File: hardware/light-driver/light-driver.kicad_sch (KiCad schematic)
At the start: 50 parts, among them J1 LED-strip0, J2 Power/CAN, J3 LED-strip1, J4 Power/CAN, J5 SWD, J6 Conn_01x08_Pin, J7 ARGB, J8 Conn_01x04_Pin, U1 TC1185-xCT, U2 TPP361061-T6TR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

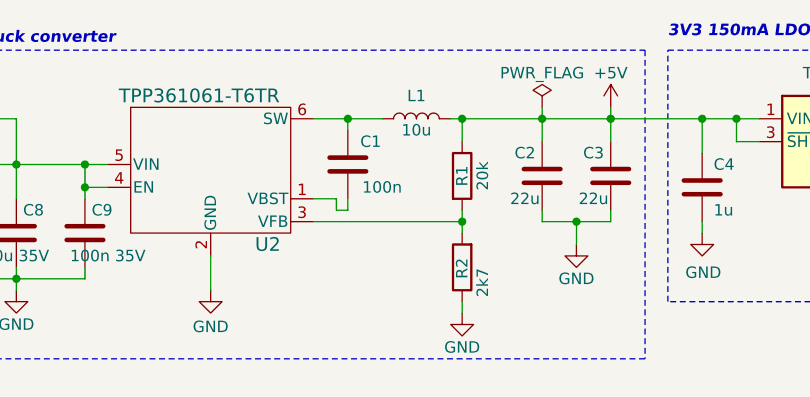
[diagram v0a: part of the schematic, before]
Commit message: Update footprints to given in inventory
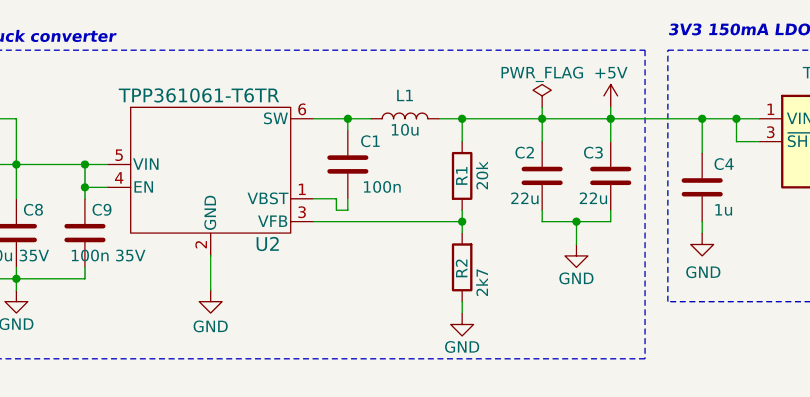
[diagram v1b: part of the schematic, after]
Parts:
- C11, C13, C2, C3, C4, C6: footprint Capacitor_SMD:C_0603_1608Metric_Pad1.08x0.95mm_HandSolder -> Capacitor_SMD:C_0805_2012Metric_Pad1.18x1.45mm_HandSolder
- L1: footprint Inductor_SMD:L_1008_2520Metric_Pad1.43x2.20mm_HandSolder -> Inductor_SMD:L_1210_3225Metric_Pad1.42x2.65mm_HandSolder
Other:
- moved on the sheet: L1
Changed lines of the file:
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@@
 	(wire
 		(pts
-			(xy 105.41 24.13) (xy 109.22 24.13)
+			(xy 105.41 24.13) (xy 107.95 24.13)
 		)
 		(stroke
@@
 	(wire
 		(pts
-			(xy 116.84 24.13) (xy 118.11 24.13)
+			(xy 115.57 24.13) (xy 118.11 24.13)
 		)
 		(stroke
@@
 			)
 		)
-		(property "Footprint" "Capacitor_SMD:C_0603_1608Metric_Pad1.08x0.95mm_HandSolder"
+		(property "Footprint" "Capacitor_SMD:C_0805_2012Metric_Pad1.18x1.45mm_HandSolder"
 			(at 208.5848 140.97 0)
 			(effects
@@
 			)
 		)
-		(property "Footprint" "Capacitor_SMD:C_0603_1608Metric_Pad1.08x0.95mm_HandSolder"
+		(property "Footprint" "Capacitor_SMD:C_0805_2012Metric_Pad1.18x1.45mm_HandSolder"
 			(at 133.6548 26.67 0)
 			(effects
@@
 			)
 		)
-		(property "Footprint" "Capacitor_SMD:C_0603_1608Metric_Pad1.08x0.95mm_HandSolder"
+		(property "Footprint" "Capacitor_SMD:C_0805_2012Metric_Pad1.18x1.45mm_HandSolder"
 			(at 188.9252 148.59 0)
 			(effects
@@
 	(symbol
 		(lib_id "Device:L")
-		(at 113.03 24.13 90)
+		(at 111.76 24.13 90)
 		(unit 1)
 		(exclude_from_sim no)
@@
 		(dnp no)
 		(property "Reference" "L1"
-			(at 113.03 21.59 90)
+			(at 111.76 21.59 90)
 			(effects
 				(font
@@
 		)
 		(property "Value" "10u"
-			(at 113.03 25.4 90)
+			(at 111.76 25.4 90)
 			(effects
 				(font
@@
 			)
 		)
-		(property "Footprint" "Inductor_SMD:L_1008_2520Metric_Pad1.43x2.20mm_HandSolder"
-			(at 113.03 24.13 0)
+		(property "Footprint" "Inductor_SMD:L_1210_3225Metric_Pad1.42x2.65mm_HandSolder"
+			(at 111.76 24.13 0)
 			(effects
 				(font
@@
 		)
 		(property "Datasheet" "~"
-			(at 113.03 24.13 0)
+			(at 111.76 24.13 0)
 			(effects
 				(font
@@
 		)
 		(property "Description" "Inductor"
-			(at 113.03 24.13 0)
+			(at 111.76 24.13 0)
 			(effects
 				(font
@@
 			)
 		)
-		(property "Footprint" "Capacitor_SMD:C_0603_1608Metric_Pad1.08x0.95mm_HandSolder"
+		(property "Footprint" "Capacitor_SMD:C_0805_2012Metric_Pad1.18x1.45mm_HandSolder"
 			(at 145.7452 35.56 0)
 			(effects
@@
 			)
 		)
-		(property "Footprint" "Capacitor_SMD:C_0603_1608Metric_Pad1.08x0.95mm_HandSolder"
+		(property "Footprint" "Capacitor_SMD:C_0805_2012Metric_Pad1.18x1.45mm_HandSolder"
 			(at 182.5752 35.56 0)
 			(effects
@@
 			)
 		)
-		(property "Footprint" "Capacitor_SMD:C_0603_1608Metric_Pad1.08x0.95mm_HandSolder"
+		(property "Footprint" "Capacitor_SMD:C_0805_2012Metric_Pad1.18x1.45mm_HandSolder"
 			(at 126.0348 26.67 0)
 			(effects

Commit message: Add notes
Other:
- note added: "Unless otherwise specified, the working voltage of all capacitors is 6.3V."
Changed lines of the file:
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@@
+		)
+	)
+	(text "Unless otherwise specified, the working voltage of all capacitors is 6.3V. "
+		(exclude_from_sim no)
+		(at 231.14 173.99 0)
+		(effects
+			(font
+				(size 1.8 1.8)
+			)
 		)
 	)

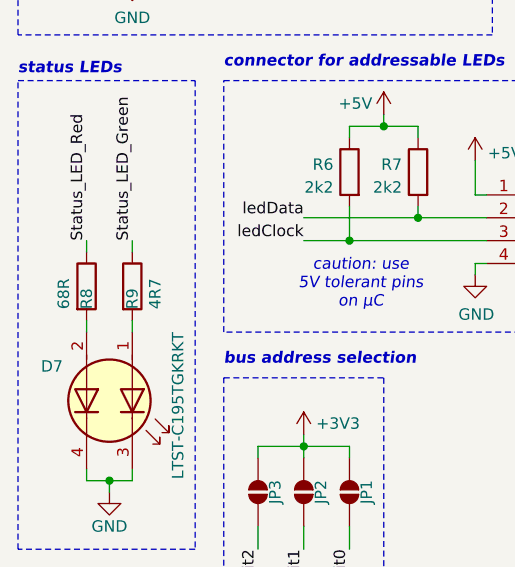
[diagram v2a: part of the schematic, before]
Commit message: Update some values
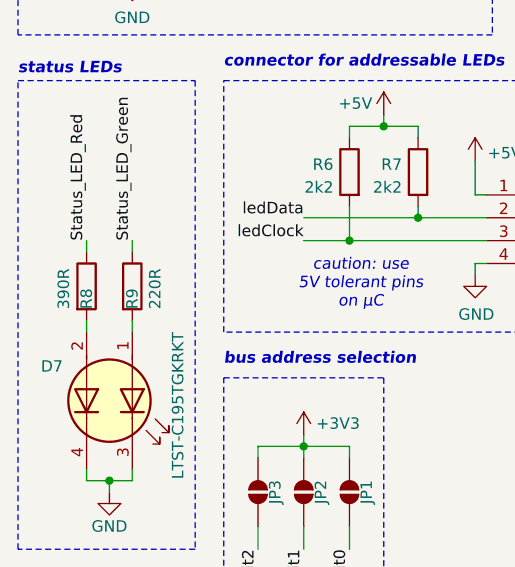
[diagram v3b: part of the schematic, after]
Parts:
- R8: value 68R -> 390R
- R9: value 4R7 -> 220R
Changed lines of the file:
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@@
 			)
 		)
-		(property "Value" "4R7"
+		(property "Value" "220R"
 			(at 30.48 138.43 90)
 			(effects
@@
 			)
 		)
-		(property "Value" "68R"
+		(property "Value" "390R"
 			(at 20.32 138.43 90)
 			(effects
